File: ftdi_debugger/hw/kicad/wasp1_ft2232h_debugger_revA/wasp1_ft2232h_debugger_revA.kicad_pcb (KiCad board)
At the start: 4 copper layers, 110 x 65 mm, 57 parts, among them J1 USB4105-GF-A, J2 WASP1 TARGET, Q1 2N7002, U1 FT2232HL, U2 93LC56BT-I/SN DNI, U3 TLV7041DBVR, U4 SN74AXC8T245PWR, U5 SN74AXC2T245RSWR, U6 AP2112K-3.3, U7 SN74LVC1G00DBVR, Y1 12MHz

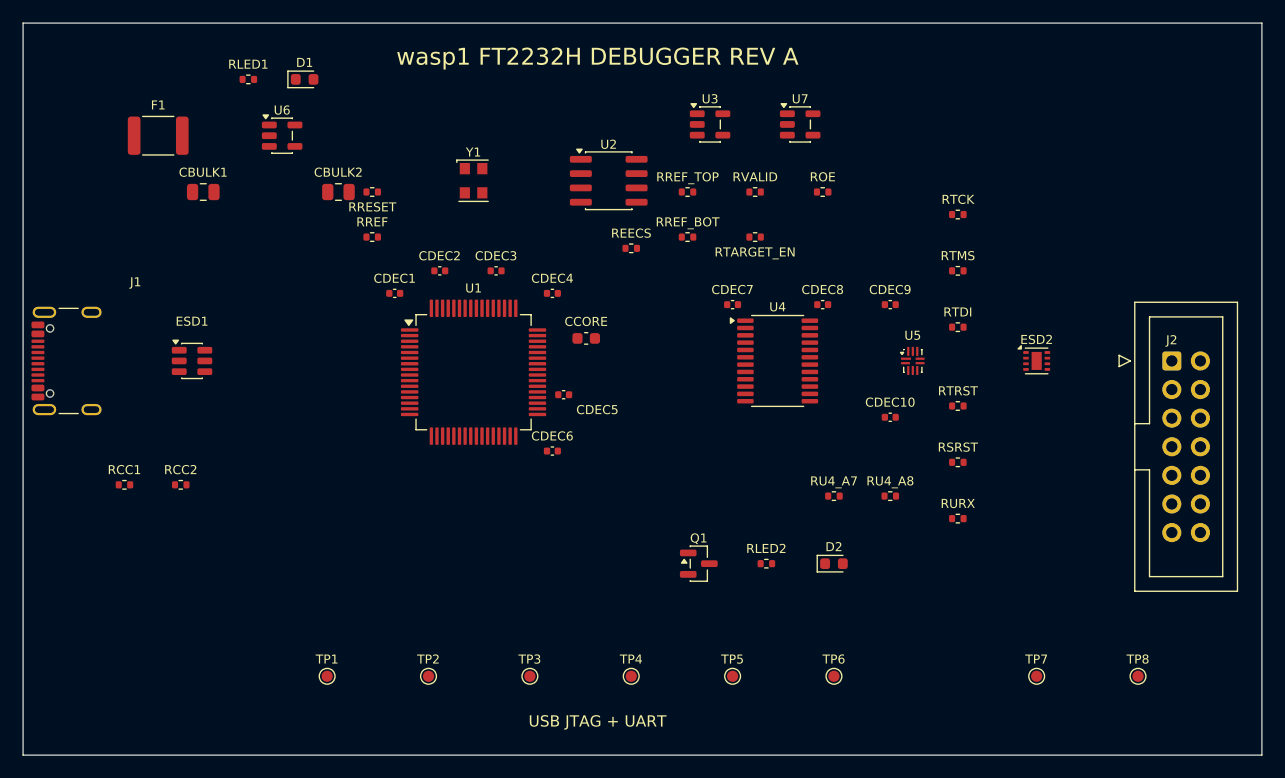
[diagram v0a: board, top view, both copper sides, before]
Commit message: Route FTDI debugger PCB
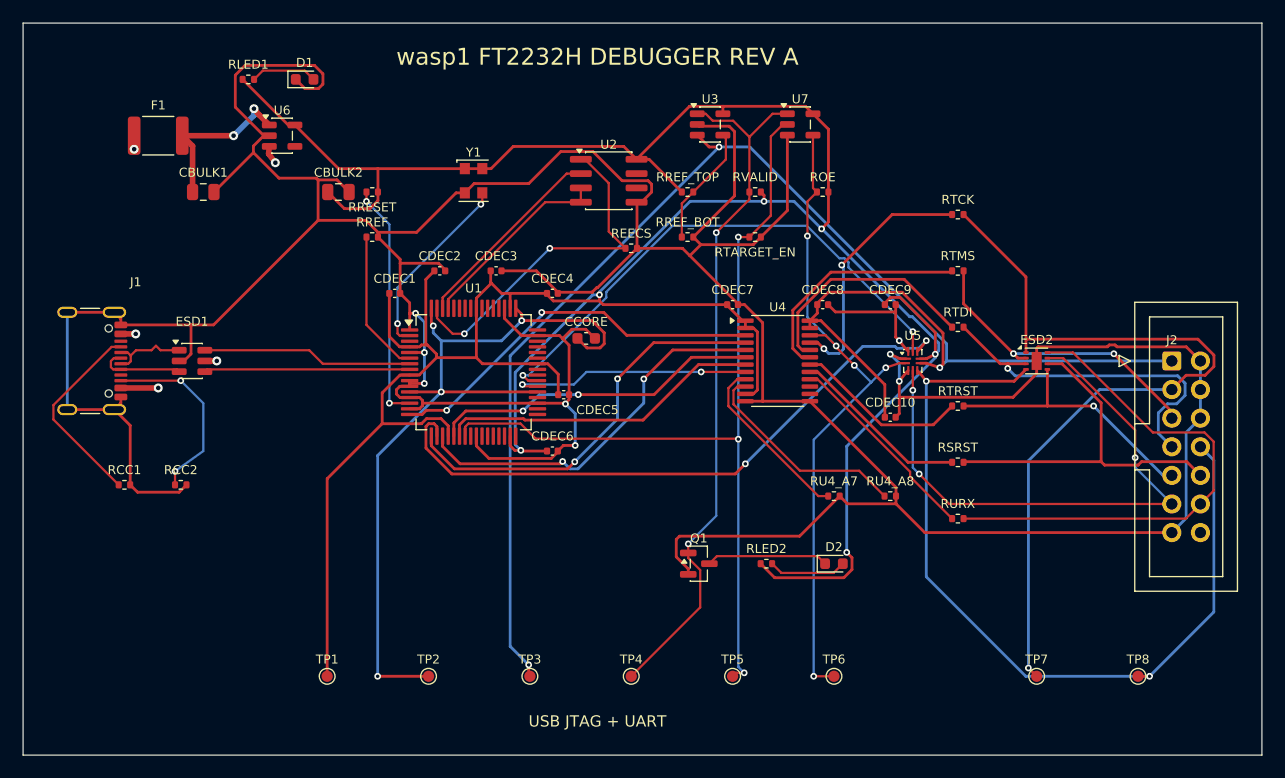
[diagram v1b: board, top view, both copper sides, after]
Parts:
- turned J1 to -90 degrees
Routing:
- net GND: track 0.00 -> 415.6 mm, vias 0 -> 8
- net VCC_3V3: track 0.00 -> 298.5 mm, vias 0 -> 6
- net VREF: track 0.00 -> 140.1 mm, vias 0 -> 3
- net FT_TARGET_EN: track 0.00 -> 78.5 mm, vias 0 -> 3
- net TDO: track 0.00 -> 75.6 mm, vias 0 -> 2
- net TCK: track 0.00 -> 72.2 mm, vias 0 -> 1
- net VCORE: track 0.00 -> 72.1 mm, vias 0 -> 4
- net VREF_VALID: track 0.00 -> 62.8 mm, vias 0 -> 2
- net SHIFT_OE_N: track 0.00 -> 61.2 mm, vias 0 -> 5
- net FT_A_TDO: track 0.00 -> 55.6 mm, vias 0 -> 2
- net UART_TXD: track 0.00 -> 51.3 mm, vias 0 -> 3
- net FT_B_RXD: track 0.00 -> 47.8 mm, vias 0 -> 2
- net UART_RXD: track 0.00 -> 45.6 mm
- net USB_VBUS: track 0.00 -> 37.4 mm, vias 0 -> 4
- net FT_A_TDI: track 0.00 -> 36.3 mm, vias 0 -> 2
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- added copper zone on In1.Cu, net GND
